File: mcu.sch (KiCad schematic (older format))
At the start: 27 parts, among them J4 Conn_ARM_JTAG_SWD_10, Y1 25MHz

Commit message: Updated the MCU
Updated the MCU to one that is on JLCPCB so that I can get it ordered from JLCPCB.
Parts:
- removed C14: 2.2u, symbol Device:C_Small
- removed J4: Conn_ARM_JTAG_SWD_10, symbol Connector:Conn_ARM_JTAG_SWD_10
- removed U?: STM32F401CBUx, Package_DFN_QFN:QFN-48-1EP_7x7mm_P0.5mm_EP5.6x5.6mm, symbol MCU_ST_STM32F4:STM32F401CBUx
- added C?: C_Small, symbol Device:C_Small
- added J?: Conn_ARM_JTAG_SWD_20, symbol Connector:Conn_ARM_JTAG_SWD_20
- added U?: STM32F401RCTx, Package_QFP:LQFP-64_10x10mm_P0.5mm, symbol MCU_ST_STM32F4:STM32F401RCTx
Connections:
- net labels added: JTCK, JTDI, JTDO, JTMS, JTRST, NJTRST, SDIO_CK, SDIO_CMD, SDIO_D0, SDIO_D1, SDIO_D2, SDIO_D3
- net labels removed: BAUD_RATE, BT_DISCOVERY_MODE, BT_FACTORY_RESET, BT_GPIO9, BT_MODE, BT_REMOTE_DTR, BT_REMOTE_RTS, BT_UART_ACTIVITY, SYS_ITCK-SWCLK, SYS_ITDO-SWCLK, SYS_ITDO-SWO, SYS_ITMS-SWDIO, uSD_MISO, uSD_MOSI, uSD_SCLK
- wire segments 120 -> 131
- no-connect marks 1 -> 26
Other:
- note added: "Media Controls"
- moved on the sheet: C12, C13, C?, R4, R?, SW?, Y1

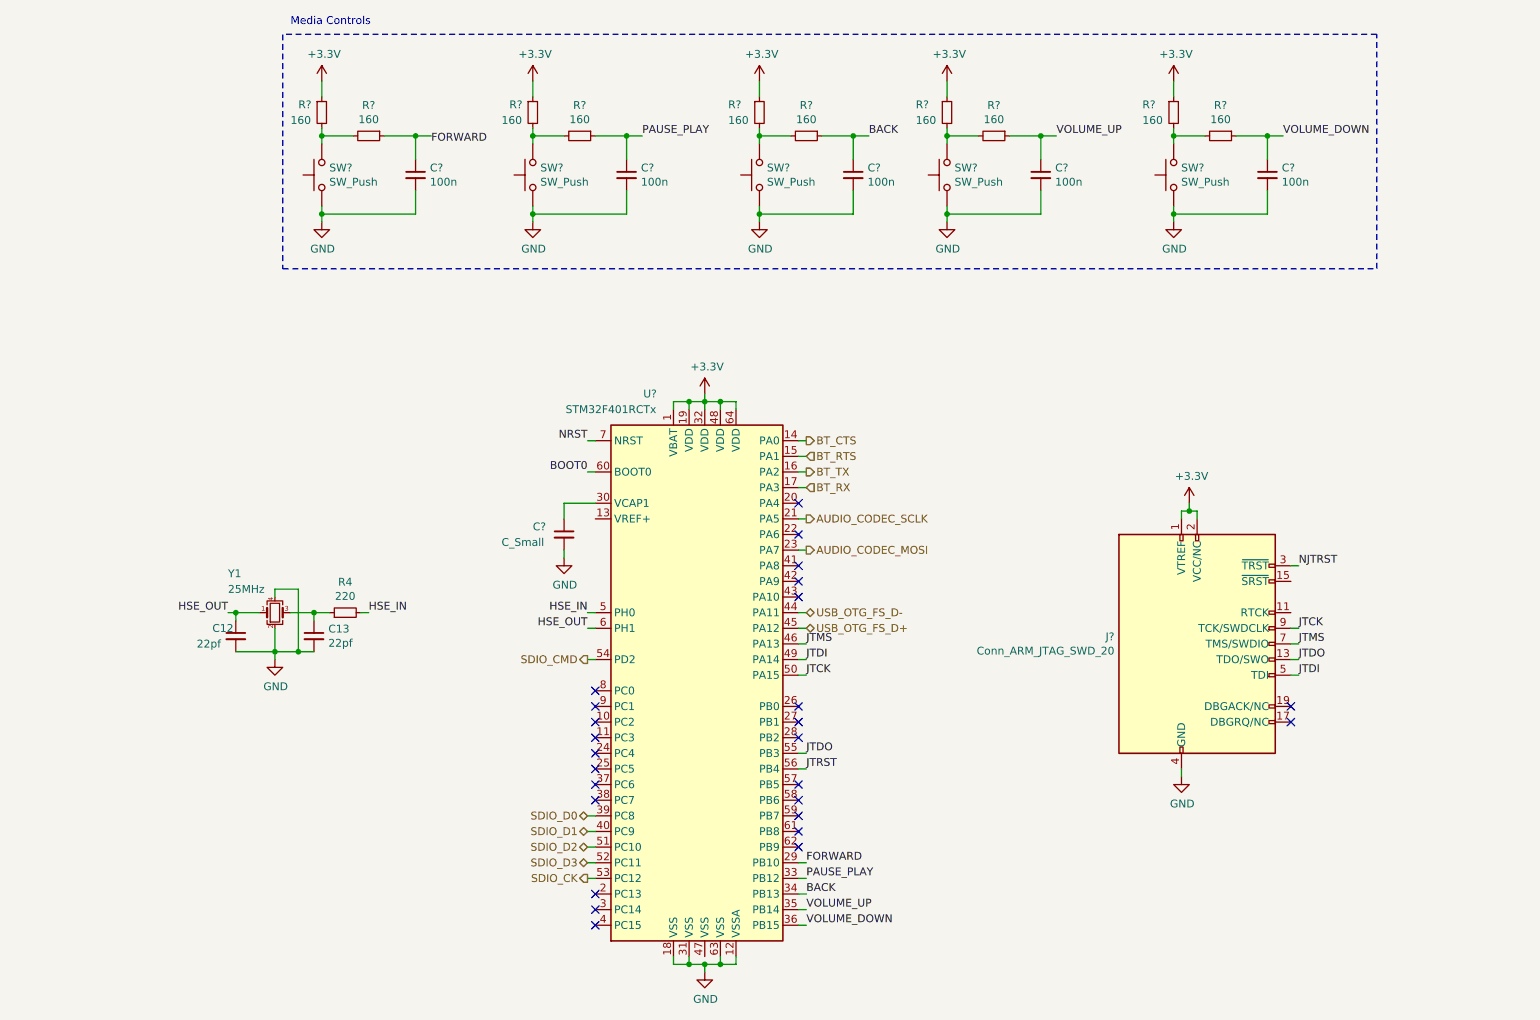
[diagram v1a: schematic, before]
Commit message: Updated footprints
Updated some parts to JLCPCB SMT library and also added some footprints
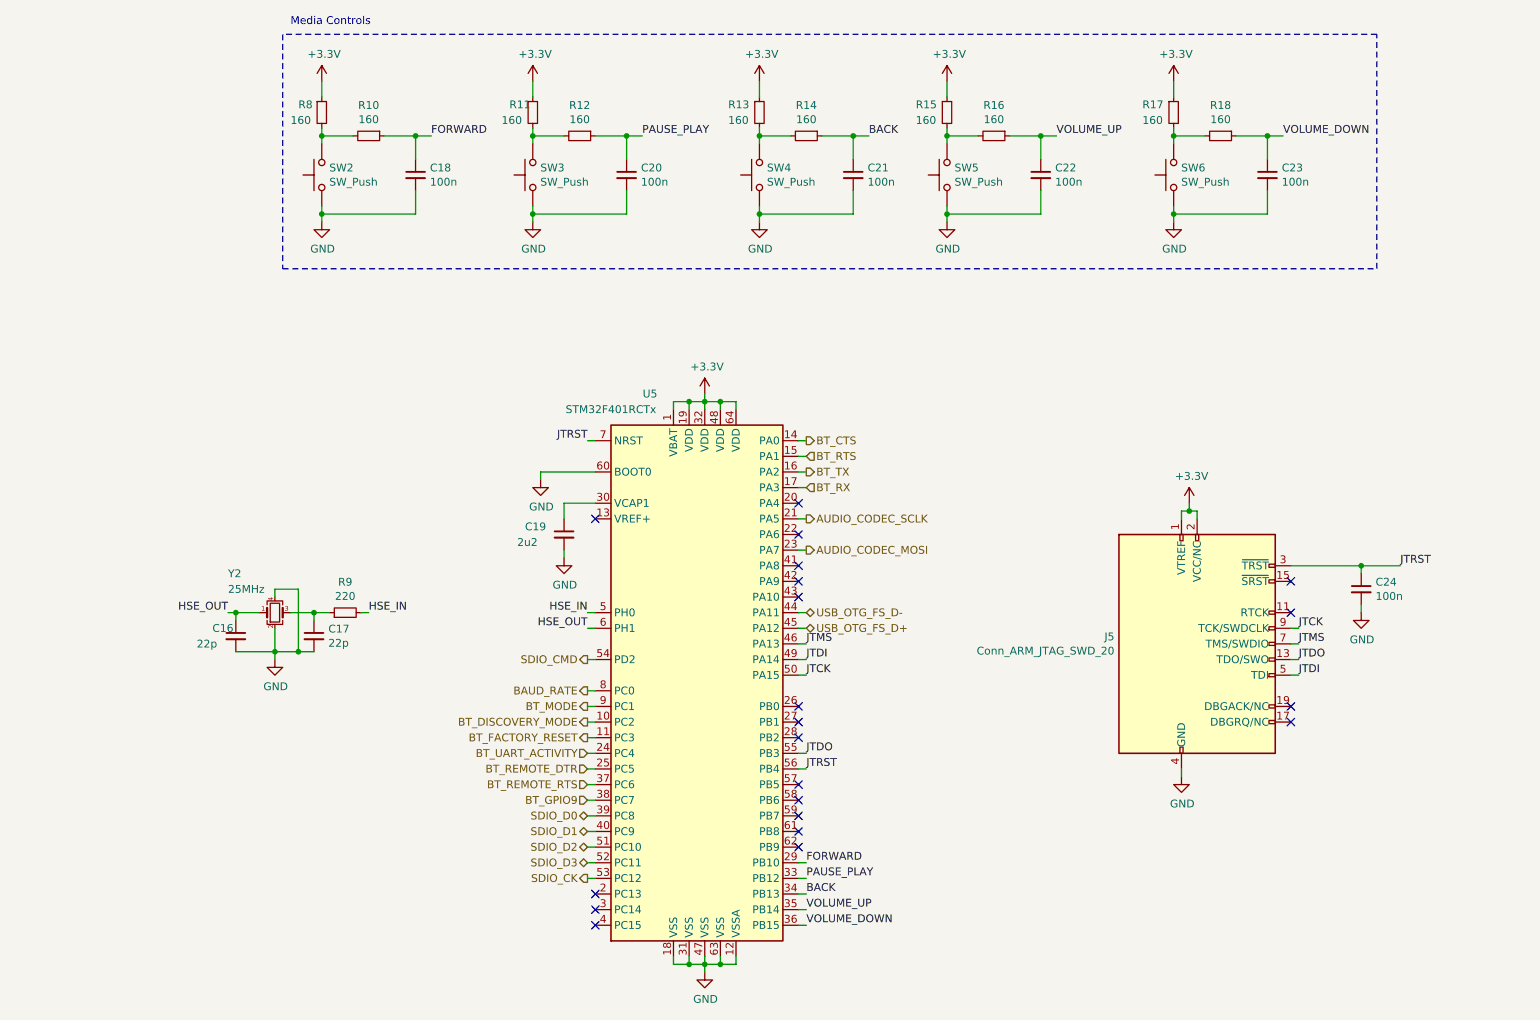
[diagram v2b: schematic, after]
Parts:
- added C24: 100n, Capacitor_SMD:C_0402_1005Metric, symbol Device:C_Small
- C16: renamed from C12; value 22pf -> 22p; footprint (none) -> Capacitor_SMD:C_0805_2012Metric
- C17: renamed from C13; value 22pf -> 22p; footprint (none) -> Capacitor_SMD:C_0805_2012Metric
- C18, C20, C21, C22, C23: renamed from C?; footprint (none) -> Capacitor_SMD:C_0402_1005Metric
- C19: renamed from C?; value C_Small -> 2u2; footprint (none) -> Capacitor_SMD:C_0603_1608Metric
- J5: renamed from J?; footprint (none) -> Connector_Samtec:Samtec_LSHM-110-xx.x-x-DV-N_2x10_P0.50mm_Vertical
- gave numbers to parts that had none: 16
- renumbered R4 to R9, Y1 to Y2
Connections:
- net BOOT0 is gone; now on net GND: U5.60 (BOOT0)
- net NJTRST is gone; now on net JTRST: J5.3 (~TRST~)
- net NRST is gone; now on net JTRST: U5.7 (NRST)
- net FORWARD: now also C18.1, R10.1
- net GND: now also U5.47 (VSS), C24.2
- net JTRST: now also C24.1
- net BT_DISCOVERY_MODE: now reaches U5.10 (PC2)
- net BT_FACTORY_RESET: now reaches U5.11 (PC3)
- net BT_UART_ACTIVITY: now reaches U5.24 (PC4)
- net BT_REMOTE_DTR: now reaches U5.25 (PC5)
- net BT_REMOTE_RTS: now reaches U5.37 (PC6)
- net BT_GPIO9: now reaches U5.38 (PC7)
- net BAUD_RATE: now reaches U5.8 (PC0)
- net BT_MODE: now reaches U5.9 (PC1)
- no-connect marks 26 -> 21

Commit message: Update footprints
Add footprints for resistors, push buttons, regulator, and crystals
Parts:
- R10, R11, R12, R13, R14, R15, R16, R17, R18, R8, R9: footprint (none) -> Resistor_SMD:R_0603_1608Metric
- SW2, SW3, SW4, SW5, SW6: footprint (none) -> Button_Switch_THT:SW_DIP_SPSTx01_Piano_10.8x4.1mm_W7.62mm_P2.54mm
- Y2: footprint (none) -> Crystal:Crystal_SMD_3225-4Pin_3.2x2.5mm
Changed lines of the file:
@@
 F 0 "SW2" V 2746 1852 50  0000 R CNN
 F 1 "SW_Push" V 2655 1852 50  0000 R CNN
-F 2 "" H 2700 2100 50  0001 C CNN
+F 2 "Button_Switch_THT:SW_DIP_SPSTx01_Piano_10.8x4.1mm_W7.62mm_P2.54mm" H 2700 2100 50  0001 C CNN
 F 3 "~" H 2700 2100 50  0001 C CNN
 	1    2700 1900
@@
 F 0 "R8" H 2550 1550 50  0000 L CNN
 F 1 "160" H 2500 1450 50  0000 L CNN
-F 2 "" H 2700 1500 50  0001 C CNN
+F 2 "Resistor_SMD:R_0603_1608Metric" H 2700 1500 50  0001 C CNN
 F 3 "~" H 2700 1500 50  0001 C CNN
 	1    2700 1500
@@
 F 0 "R10" V 2804 1650 50  0000 C CNN
 F 1 "160" V 2895 1650 50  0000 C CNN
-F 2 "" H 3000 1650 50  0001 C CNN
+F 2 "Resistor_SMD:R_0603_1608Metric" H 3000 1650 50  0001 C CNN
 F 3 "~" H 3000 1650 50  0001 C CNN
 	1    3000 1650
@@
 F 0 "SW3" V 4096 1852 50  0000 R CNN
 F 1 "SW_Push" V 4005 1852 50  0000 R CNN
-F 2 "" H 4050 2100 50  0001 C CNN
+F 2 "Button_Switch_THT:SW_DIP_SPSTx01_Piano_10.8x4.1mm_W7.62mm_P2.54mm" H 4050 2100 50  0001 C CNN
 F 3 "~" H 4050 2100 50  0001 C CNN
 	1    4050 1900
@@
 F 0 "R11" H 3900 1550 50  0000 L CNN
 F 1 "160" H 3850 1450 50  0000 L CNN
-F 2 "" H 4050 1500 50  0001 C CNN
+F 2 "Resistor_SMD:R_0603_1608Metric" H 4050 1500 50  0001 C CNN
 F 3 "~" H 4050 1500 50  0001 C CNN
 	1    4050 1500
@@
 F 0 "R12" V 4154 1650 50  0000 C CNN
 F 1 "160" V 4245 1650 50  0000 C CNN
-F 2 "" H 4350 1650 50  0001 C CNN
+F 2 "Resistor_SMD:R_0603_1608Metric" H 4350 1650 50  0001 C CNN
 F 3 "~" H 4350 1650 50  0001 C CNN
 	1    4350 1650
@@
 F 0 "R18" V 8254 1650 50  0000 C CNN
 F 1 "160" V 8345 1650 50  0000 C CNN
-F 2 "" H 8450 1650 50  0001 C CNN
+F 2 "Resistor_SMD:R_0603_1608Metric" H 8450 1650 50  0001 C CNN
 F 3 "~" H 8450 1650 50  0001 C CNN
 	1    8450 1650
@@
 F 0 "R17" H 7950 1550 50  0000 L CNN
 F 1 "160" H 7950 1450 50  0000 L CNN
-F 2 "" H 8150 1500 50  0001 C CNN
+F 2 "Resistor_SMD:R_0603_1608Metric" H 8150 1500 50  0001 C CNN
 F 3 "~" H 8150 1500 50  0001 C CNN
 	1    8150 1500
@@
 F 0 "SW6" V 8196 1852 50  0000 R CNN
 F 1 "SW_Push" V 8105 1852 50  0000 R CNN
-F 2 "" H 8150 2100 50  0001 C CNN
+F 2 "Button_Switch_THT:SW_DIP_SPSTx01_Piano_10.8x4.1mm_W7.62mm_P2.54mm" H 8150 2100 50  0001 C CNN
 F 3 "~" H 8150 2100 50  0001 C CNN
 	1    8150 1900
@@
 F 0 "R16" V 6804 1650 50  0000 C CNN
 F 1 "160" V 6895 1650 50  0000 C CNN
-F 2 "" H 7000 1650 50  0001 C CNN
+F 2 "Resistor_SMD:R_0603_1608Metric" H 7000 1650 50  0001 C CNN
 F 3 "~" H 7000 1650 50  0001 C CNN
 	1    7000 1650
@@
 F 0 "R15" H 6500 1550 50  0000 L CNN
 F 1 "160" H 6500 1450 50  0000 L CNN
-F 2 "" H 6700 1500 50  0001 C CNN
+F 2 "Resistor_SMD:R_0603_1608Metric" H 6700 1500 50  0001 C CNN
 F 3 "~" H 6700 1500 50  0001 C CNN
 	1    6700 1500
@@
 F 0 "SW5" V 6746 1852 50  0000 R CNN
 F 1 "SW_Push" V 6655 1852 50  0000 R CNN
-F 2 "" H 6700 2100 50  0001 C CNN
+F 2 "Button_Switch_THT:SW_DIP_SPSTx01_Piano_10.8x4.1mm_W7.62mm_P2.54mm" H 6700 2100 50  0001 C CNN
 F 3 "~" H 6700 2100 50  0001 C CNN
 	1    6700 1900
@@
 F 0 "R14" V 5604 1650 50  0000 C CNN
 F 1 "160" V 5695 1650 50  0000 C CNN
-F 2 "" H 5800 1650 50  0001 C CNN
+F 2 "Resistor_SMD:R_0603_1608Metric" H 5800 1650 50  0001 C CNN
 F 3 "~" H 5800 1650 50  0001 C CNN
 	1    5800 1650
@@
 F 0 "R13" H 5300 1550 50  0000 L CNN
 F 1 "160" H 5300 1450 50  0000 L CNN
-F 2 "" H 5500 1500 50  0001 C CNN
+F 2 "Resistor_SMD:R_0603_1608Metric" H 5500 1500 50  0001 C CNN
 F 3 "~" H 5500 1500 50  0001 C CNN
 	1    5500 1500
@@
 F 0 "SW4" V 5546 1852 50  0000 R CNN
 F 1 "SW_Push" V 5455 1852 50  0000 R CNN
-F 2 "" H 5500 2100 50  0001 C CNN
+F 2 "Button_Switch_THT:SW_DIP_SPSTx01_Piano_10.8x4.1mm_W7.62mm_P2.54mm" H 5500 2100 50  0001 C CNN
 F 3 "~" H 5500 2100 50  0001 C CNN
 	1    5500 1900
@@
 F 0 "Y2" H 2100 4950 50  0000 L CNN
 F 1 "25MHz" H 2100 4850 50  0000 L CNN
-F 2 "" H 2400 4700 50  0001 C CNN
+F 2 "Crystal:Crystal_SMD_3225-4Pin_3.2x2.5mm" H 2400 4700 50  0001 C CNN
 F 3 "~" H 2400 4700 50  0001 C CNN
 	1    2400 4700
@@
 F 0 "R9" V 3046 4700 50  0000 C CNN
 F 1 "220" V 2955 4700 50  0000 C CNN
-F 2 "" H 2850 4700 50  0001 C CNN
+F 2 "Resistor_SMD:R_0603_1608Metric" H 2850 4700 50  0001 C CNN
 F 3 "~" H 2850 4700 50  0001 C CNN
 	1    2850 4700

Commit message: Updating parts
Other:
- moved on the sheet: C16, C17, R9, Y2
